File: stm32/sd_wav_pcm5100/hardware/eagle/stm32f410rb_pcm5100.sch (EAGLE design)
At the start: 33 parts, among them IC1 STM32F410_8_B_LQFP64, U5 ROBERTSONICS_PCM5100

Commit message: added shenzen2u/smart-proto cam/dru files
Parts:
- IC1: value STM32F410_8_B_LQFP64 -> STM32F410
- U5: value ROBERTSONICS_PCM5100 -> PCM5100
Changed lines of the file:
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@@
 </classes>
 <parts>
-<part name="U5" library="stm32f410rb_pcm5100" deviceset="ROBERTSONICS_PCM5100" device=""/>
+<part name="U5" library="stm32f410rb_pcm5100" deviceset="ROBERTSONICS_PCM5100" device="" value="PCM5100"/>
 <part name="C21" library="SparkFun-Passives" deviceset="CAP" device="0805" value="0.1uF"/>
 <part name="C22" library="SparkFun-Passives" deviceset="CAP" device="0805" value="0.1uF"/>
@@
 <part name="JP5" library="SparkFun-Connectors" deviceset="M03" device="SCREW" value="BTN_5-7"/>
 <part name="JP6" library="SparkFun-Connectors" deviceset="M04" device="SCREW" value="AUDIO_OUT"/>
-<part name="IC1" library="pel_stm32" deviceset="STM32F410_8_B_LQFP64" device=""/>
+<part name="IC1" library="pel_stm32" deviceset="STM32F410_8_B_LQFP64" device="" value="STM32F410"/>
 <part name="JP2" library="SparkFun-Connectors" deviceset="M02" device="3.5MM" value="Vsupply - 3.3Vcc"/>
 <part name="P+4" library="supply1" deviceset="VCC" device="" value="+3V3"/>

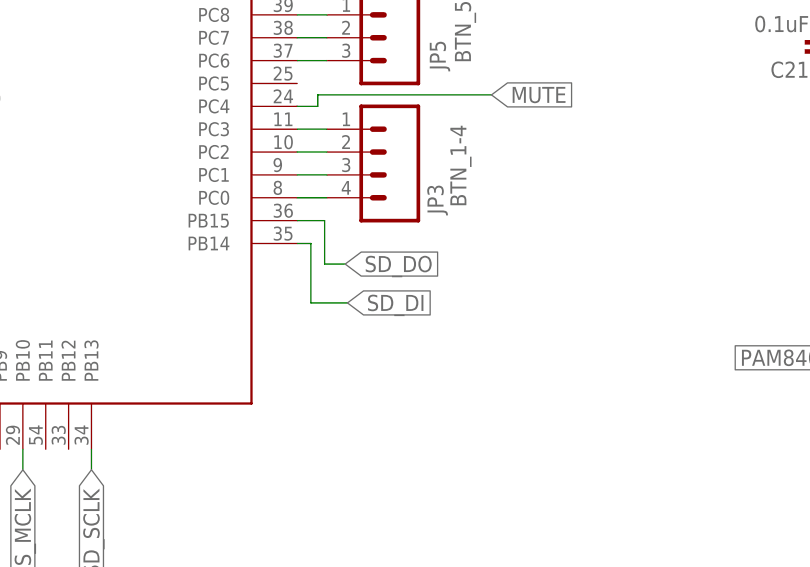
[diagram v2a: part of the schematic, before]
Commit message: [stm32/sd_wav_pcm5100] SPI DI/DO lines were inversed
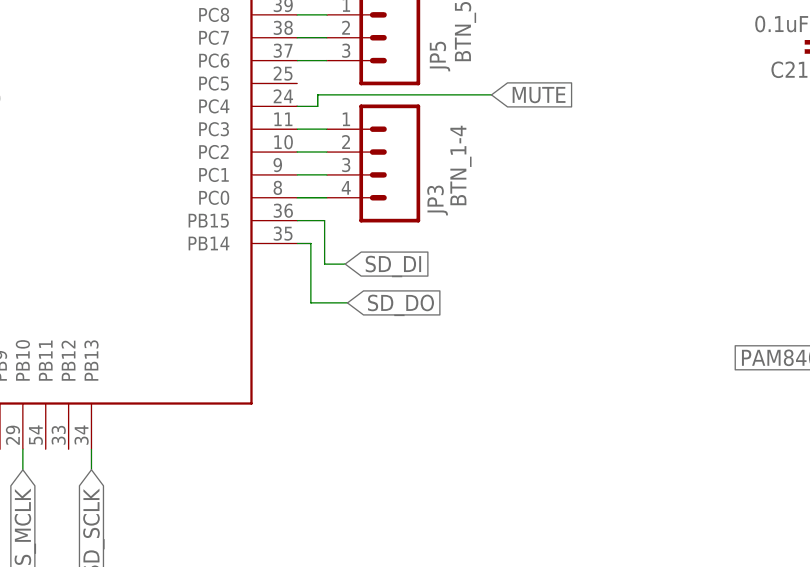
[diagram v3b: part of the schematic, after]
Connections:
- net SD_DI: now also IC1.PB15; no longer IC1.PB14
- net SD_DO: now also IC1.PB14; no longer IC1.PB15
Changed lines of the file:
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@@
+</segment>
+<segment>
+<wire x1="132.842" y1="59.182" x2="135.89" y2="59.182" width="0.1524" layer="91"/>
+<wire x1="135.89" y1="59.182" x2="135.89" y2="54.356" width="0.1524" layer="91"/>
+<wire x1="135.89" y1="54.356" x2="138.176" y2="54.356" width="0.1524" layer="91"/>
+<label x="138.176" y="54.356" size="1.778" layer="95" xref="yes"/>
+<pinref part="IC1" gate="G$1" pin="PB15"/>
+</segment>
+</net>
+<net name="SD_DO" class="0">
+<segment>
+<pinref part="MMC1" gate="G$1" pin="DAT0"/>
+<wire x1="135.89" y1="136.906" x2="129.794" y2="136.906" width="0.1524" layer="91"/>
+<label x="129.794" y="136.906" size="1.778" layer="95" rot="R180" xref="yes"/>
 </segment>
 <segment>
@@
 </segment>
 </net>
-<net name="SD_DO" class="0">
-<segment>
-<pinref part="MMC1" gate="G$1" pin="DAT0"/>
-<wire x1="135.89" y1="136.906" x2="129.794" y2="136.906" width="0.1524" layer="91"/>
-<label x="129.794" y="136.906" size="1.778" layer="95" rot="R180" xref="yes"/>
-</segment>
-<segment>
-<wire x1="132.842" y1="59.182" x2="135.89" y2="59.182" width="0.1524" layer="91"/>
-<wire x1="135.89" y1="59.182" x2="135.89" y2="54.356" width="0.1524" layer="91"/>
-<wire x1="135.89" y1="54.356" x2="138.176" y2="54.356" width="0.1524" layer="91"/>
-<label x="138.176" y="54.356" size="1.778" layer="95" xref="yes"/>
-<pinref part="IC1" gate="G$1" pin="PB15"/>
-</segment>
-</net>
